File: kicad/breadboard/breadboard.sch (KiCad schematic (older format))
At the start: 111 parts, among them J1 1, J10 2, J100 Conn_01x02, J101 Conn_01x02, J102 Conn_01x02, J103 Conn_01x02, J104 Conn_01x40, J105 Conn_01x40, J11 3, J12 3, J13 1, J14 1, J15 2, J16 2, J17 3, J18 3, J19 1, J2 1, J20 1, J21 2, J22 2, J23 3, J24 3, J25 1, J26 1, J27 2, J28 2, J29 3, J3 2, J30 3, J31 1, J32 1, J33 2, J34 2, J35 3, J36 3, J37 1, J38 1, J39 2, J4 2, J40 2, J41 3, J42 3, J43 1, J44 1, J45 2, J46 2, J47 3, J48 3, J49 Barrel_Jack, J5 3, J50 Conn_01x02, J51 Conn_01x02, J52 Conn_01x02, J53 Conn_01x02, J54 Conn_01x02, J55 Conn_01x02, J56 Conn_01x02, J57 Conn_01x02, J58 Conn_01x02, J59 Conn_01x02, J6 3, J60 Conn_01x02, J61 Conn_01x02, J62 Conn_01x02, J63 Conn_01x02, J64 Conn_01x40, J65 Conn_01x40, J66 Conn_01x02, J67 Conn_01x02, J68 Conn_01x02, J69 Conn_01x02, J7 1, J70 Conn_01x02, J71 Conn_01x02, J72 Conn_01x02, J73 Conn_01x02, J74 Conn_01x02, J75 Conn_01x02, J76 Conn_01x02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

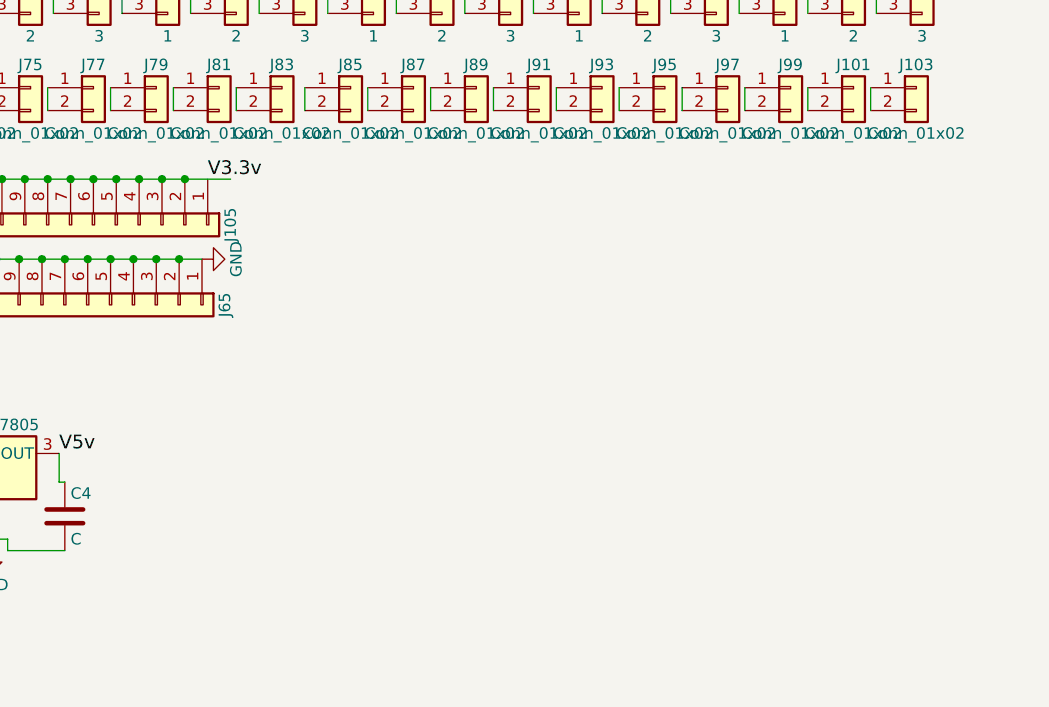
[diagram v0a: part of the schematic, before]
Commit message: breadboard: Add esp12e into board
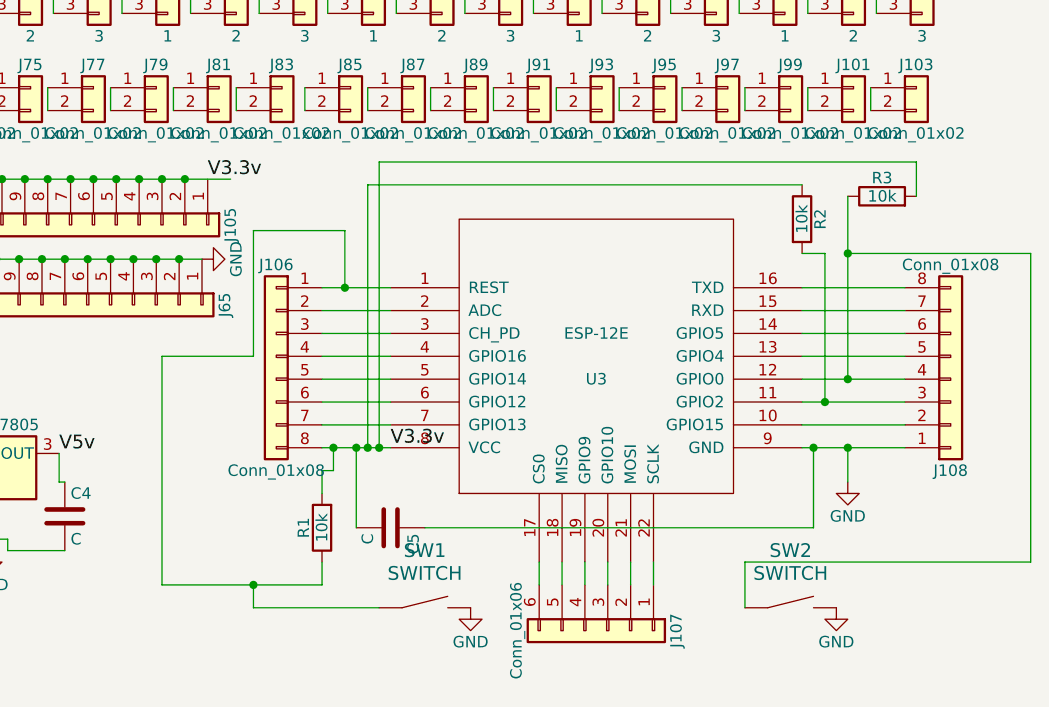
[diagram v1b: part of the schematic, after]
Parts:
- added C5: C, Capacitors_SMD:C_0603_HandSoldering, symbol C
- added J106, J108: Conn_01x08, Pin_Headers:Pin_Header_Straight_1x08_Pitch1.27mm, symbol Conn_01x08
- added J107: Conn_01x06, Pin_Headers:Pin_Header_Straight_1x06_Pitch1.27mm, symbol Conn_01x06
- added R1, R2, R3: 10k, Resistors_SMD:R_0603_HandSoldering, symbol R
- added SW1, SW2: SWITCH, Buttons_Switches_THT:SW_PUSH_6mm, symbol SWITCH
- added U3: ESP-12E, ESP8266:ESP-12E_SMD, symbol ESP-12E
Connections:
- net GND: now also C5.1, J108.1 (Pin_1), SW1.2, SW2.2, U3.9 (GND)
- net V3.3v: now also C5.2, J106.8 (Pin_8), R1.2, R2.1, R3.2, U3.8 (VCC)
- new net: J106.1 (Pin_1), R1.1, SW1.1, U3.1 (REST)
- new net: J106.2 (Pin_2), U3.2 (ADC)
- new net: J106.3 (Pin_3), U3.3 (CH_PD)
- new net: J106.4 (Pin_4), U3.4 (GPIO16)
- new net: J106.5 (Pin_5), U3.5 (GPIO14)
- new net: J106.6 (Pin_6), U3.6 (GPIO12)
- new net: J106.7 (Pin_7), U3.7 (GPIO13)
- new net: J108.2 (Pin_2), U3.10 (GPIO15)
- new net: J108.3 (Pin_3), R2.2, U3.11 (GPIO2)
- new net: J108.4 (Pin_4), R3.1, SW2.1, U3.12 (GPIO0)
- new net: J108.5 (Pin_5), U3.13 (GPIO4)
- new net: J108.6 (Pin_6), U3.14 (GPIO5)
- new net: J108.7 (Pin_7), U3.15 (RXD)
- new net: J108.8 (Pin_8), U3.16 (TXD)
- new net: J107.1 (Pin_1), U3.22 (SCLK)
- new net: J107.2 (Pin_2), U3.21 (MOSI)
- new net: J107.3 (Pin_3), U3.20 (GPIO10)
- new net: J107.4 (Pin_4), U3.19 (GPIO9)
- new net: J107.5 (Pin_5), U3.18 (MISO)
- new net: J107.6 (Pin_6), U3.17 (CS0)

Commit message: breadboard: Add bboard-3rows component
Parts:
- removed J1, J13, J14, J19, J2, J20, J25, J26, J31, J32, J37, J38, J43, J44, J7, J8: 1, Pin_Headers:Pin_Header_Straight_1x03_Pitch1.27mm, symbol Conn_01x03
- removed J10, J15, J16, J21, J22, J27, J28, J3, J33, J34, J39, J4, J40, J45, J46, J9: 2, Pin_Headers:Pin_Header_Straight_1x03_Pitch1.27mm, symbol Conn_01x03
- removed J100, J101, J102, J103, J50, J51, J52, J53, J54, J55, J56, J57, J58, J59, J60, J61, J62, J63, J66, J67, J68, J69, J70, J71, J72, J73, J74, J75, J76, J77, J78, J79, J80, J81, J82, J83, J84, J85, J86, J87, J88, J89, J90, J91, J92, J93, J94, J95, J96, J97, J98, J99: Conn_01x02, Pin_Headers:Pin_Header_Straight_1x02_Pitch1.27mm, symbol Conn_01x02
- removed J11, J12, J17, J18, J23, J24, J29, J30, J35, J36, J41, J42, J47, J48, J5, J6: 3, Pin_Headers:Pin_Header_Straight_1x03_Pitch1.27mm, symbol Conn_01x03
- added U4: bboard_3rows, symbol bboard_3rows
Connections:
- wire segments 175 -> 315
